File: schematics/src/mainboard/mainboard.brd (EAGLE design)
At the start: 58.4 x 71.8 mm, 44 parts, among them IC1 TL074P, IC2 TL074P

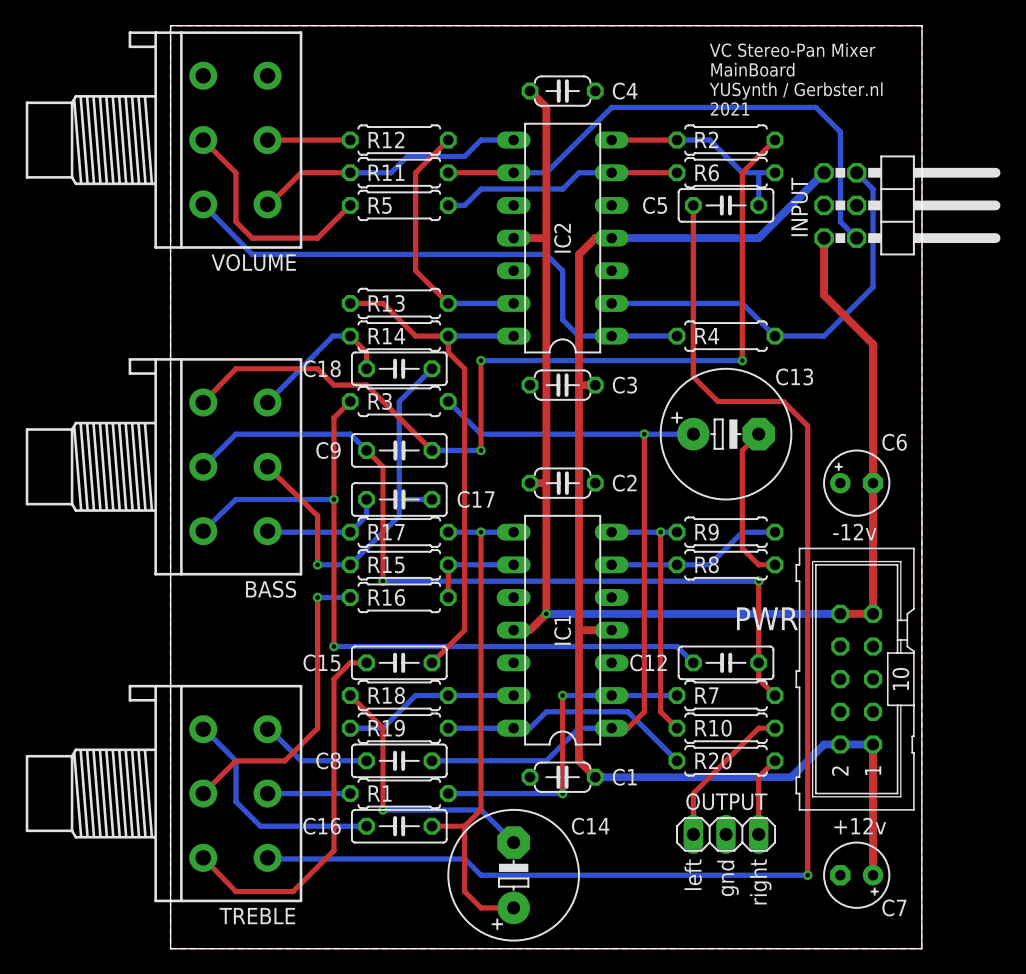
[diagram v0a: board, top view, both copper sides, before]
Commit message: Updated Schematics, Fixed Power Socket orientation
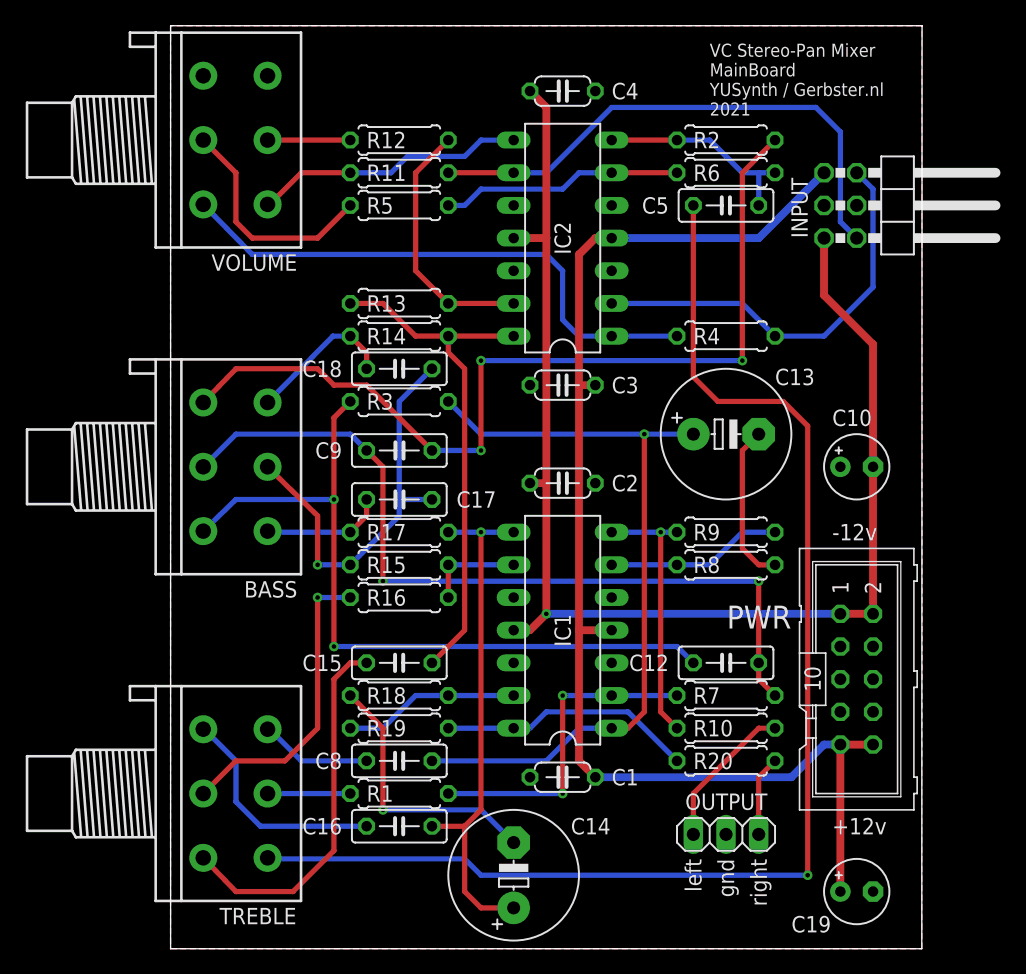
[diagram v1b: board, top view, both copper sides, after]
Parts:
- removed C6, C7: 10uf, resistor:E2,5-5
- added C10, C19: 10uf, resistor:E2,5-5
- turned PWR to 270 degrees
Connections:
- net +12V: now also C19.+, PWR.10, PWR.9; no longer C7.+, PWR.1, PWR.2
- net -12V: now also C10.-, PWR.1, PWR.2; no longer C6.-, PWR.10, PWR.9
- net GND: now also C10.+, C19.-; no longer C6.+, C7.-
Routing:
- net +12V: track 99.5 -> 100.7 mm
